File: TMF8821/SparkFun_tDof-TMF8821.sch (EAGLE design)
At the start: 27 parts, among them J4 QWIIC_RIGHT_ANGLE, J5 QWIIC_RIGHT_ANGLE

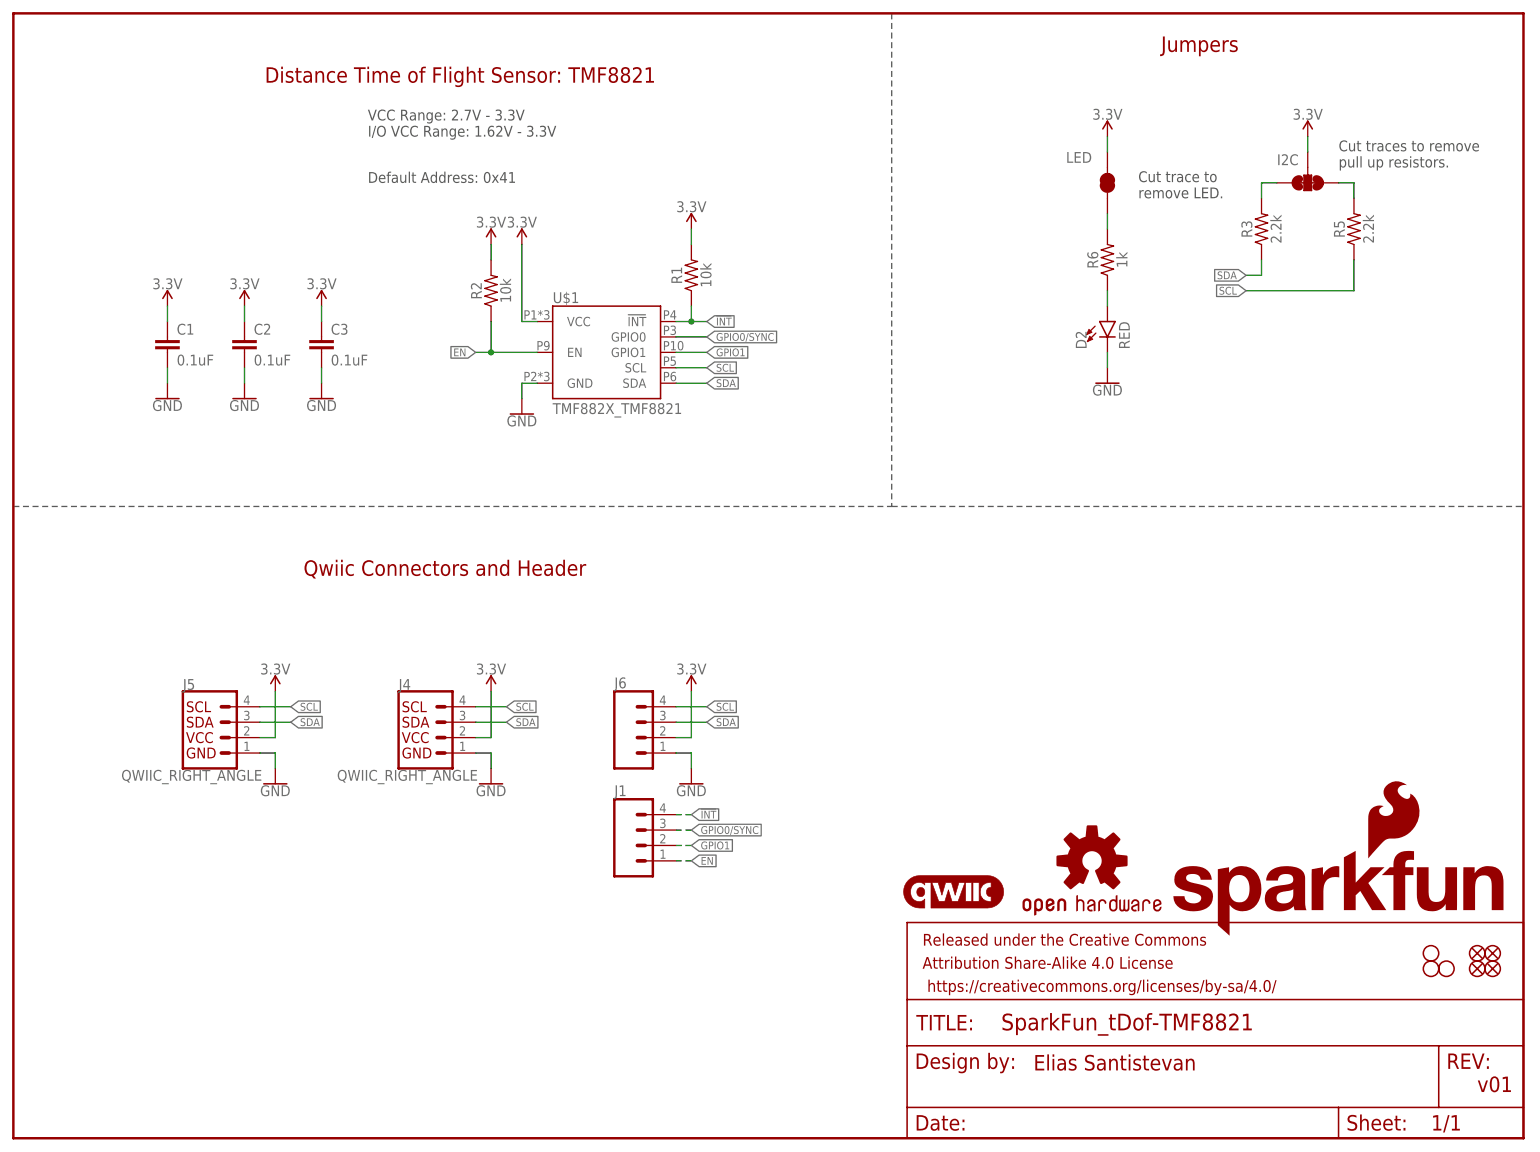
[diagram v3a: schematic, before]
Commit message: Removes old production files
* Removes old 8821 "HQ" variants
* Copies the 8820 and 8820 Mini variants
* Adjusts new 8820 copies to reference 8821 and replaces 8820 with 8821
* Updates Product Identifier jumpers to reflect changes
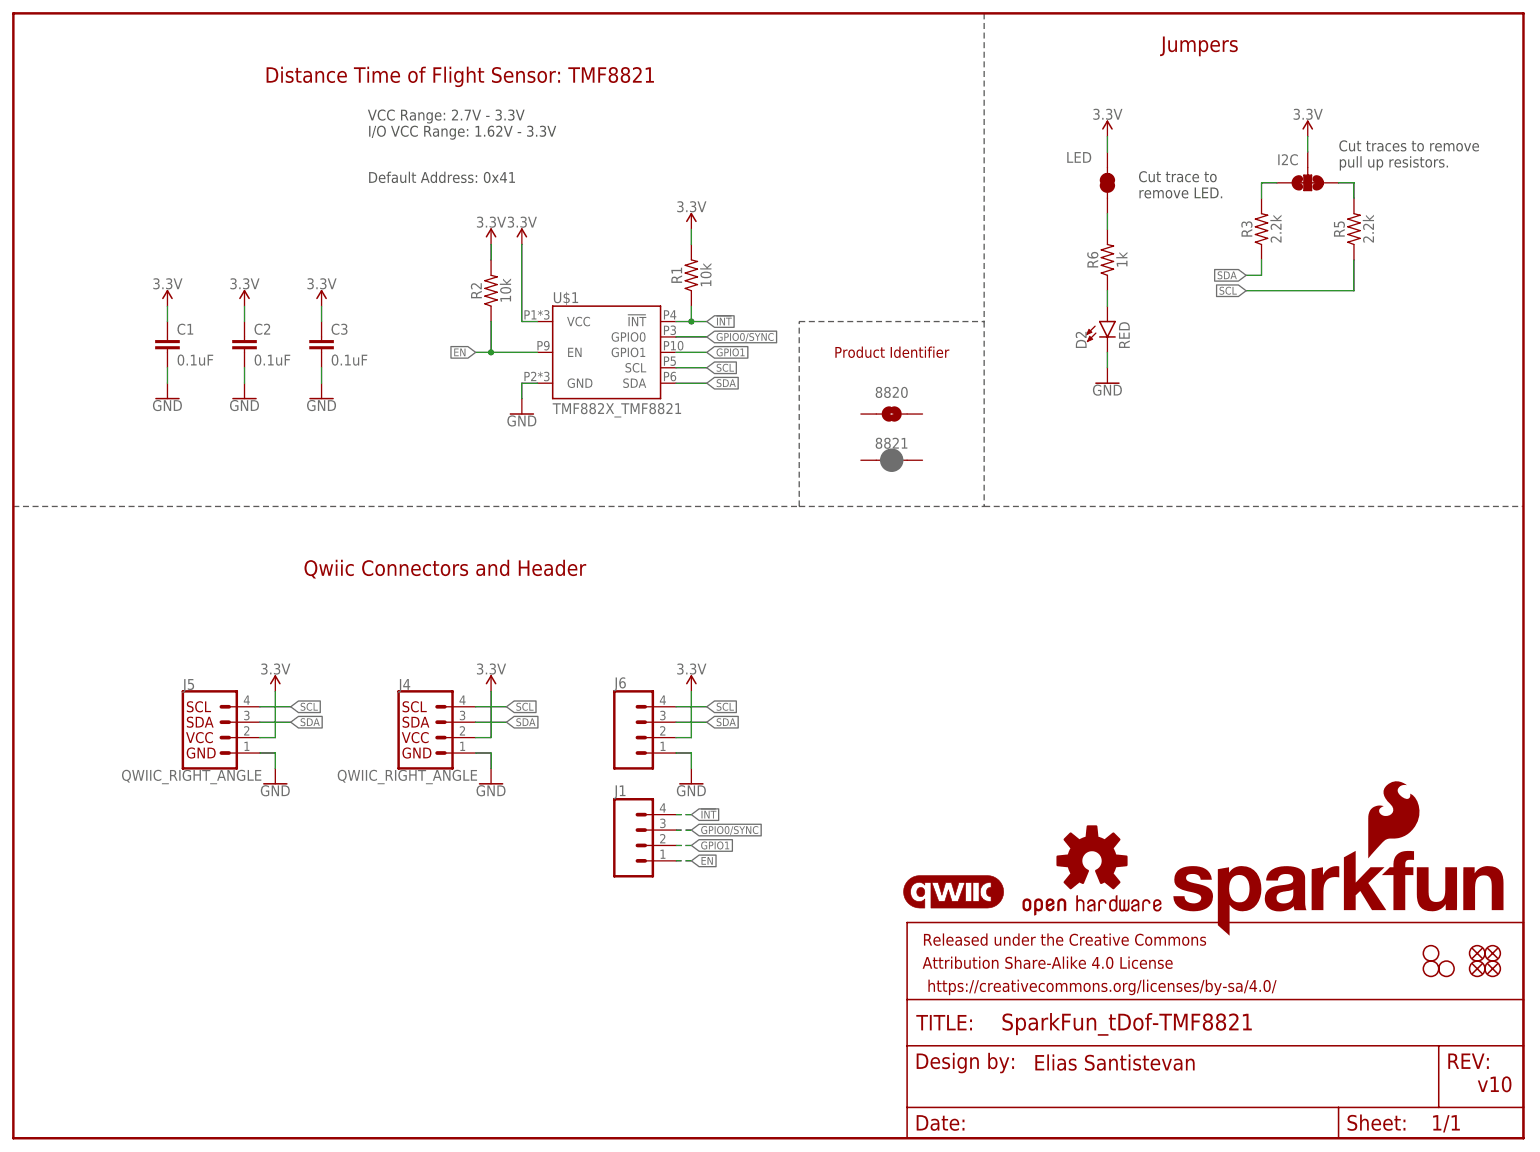
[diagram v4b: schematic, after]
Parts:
- added 8820: JUMPER-SMT_2_NO_SILK, SparkFun-Jumpers:JUMPER-SMT_2_NO_SILK
- added 8821: JUMPER-SMT_2_NC_PASTE_SILK, SparkFun-Jumpers:JUMPER-SMT_2_NC_PASTE_SILK
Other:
- note added: "Product Identifier"
- note added: "v10"
- note removed: "v01"
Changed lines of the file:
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@@
 <part name="SUPPLY11" library="SparkFun-PowerSymbols" deviceset="3.3V" device=""/>
 <part name="J1" library="SparkFun-Connectors" deviceset="CONN_04" device="1X04_NO_SILK_NO_POP"/>
+<part name="8820" library="SparkFun-Jumpers" deviceset="JUMPER-SMT_2_NO" device="_SILK" package3d_urn="urn:adsk.eagle:package:39279/1"/>
+<part name="8821" library="SparkFun-Jumpers" deviceset="JUMPER-SMT_2_NC_PASTE" device="_SILK" package3d_urn="urn:adsk.eagle:package:39282/1"/>
 </parts>
 <sheets>
 <sheet>
 <plain>
-<text x="241.3" y="7.62" size="2.54" layer="94" font="vector">v01</text>
+<text x="241.3" y="7.62" size="2.54" layer="94" font="vector">v10</text>
 <text x="71.12" y="93.98" size="2.54" layer="94" font="vector" align="center">Qwiic Connectors and Header</text>
 <text x="195.58" y="180.34" size="2.54" layer="94" font="vector" align="center">Jumpers</text>
@@
 <text x="168.148" y="11.176" size="2.54" layer="94" font="vector">Elias Santistevan</text>
 <text x="73.66" y="175.26" size="2.54" layer="94" font="vector" align="center">Distance Time of Flight Sensor: TMF8821</text>
-<wire x1="0" y1="104.14" x2="144.78" y2="104.14" width="0.2032" layer="97" style="longdash"/>
-<wire x1="144.78" y1="104.14" x2="248.92" y2="104.14" width="0.2032" layer="97" style="longdash"/>
-<wire x1="144.78" y1="185.42" x2="144.78" y2="104.14" width="0.2032" layer="97" style="longdash"/>
+<wire x1="0" y1="104.14" x2="129.54" y2="104.14" width="0.2032" layer="97" style="longdash"/>
+<wire x1="129.54" y1="104.14" x2="160.02" y2="104.14" width="0.2032" layer="97" style="longdash"/>
+<wire x1="160.02" y1="104.14" x2="248.92" y2="104.14" width="0.2032" layer="97" style="longdash"/>
+<wire x1="160.02" y1="185.42" x2="160.02" y2="134.62" width="0.2032" layer="97" style="longdash"/>
 <text x="58.42" y="165.1" size="1.778" layer="97" font="vector">VCC Range: 2.7V - 3.3V
 I/O VCC Range: 1.62V - 3.3V</text>
 <text x="58.42" y="157.48" size="1.778" layer="97" font="vector">Default Address: 0x41</text>
+<text x="144.78" y="129.54" size="1.778" layer="94" font="vector" align="center">Product Identifier</text>
+<wire x1="160.02" y1="134.62" x2="160.02" y2="104.14" width="0.2032" layer="97" style="longdash"/>
+<wire x1="129.54" y1="104.14" x2="129.54" y2="134.62" width="0.1524" layer="97" style="longdash"/>
+<wire x1="129.54" y1="134.62" x2="160.02" y2="134.62" width="0.1524" layer="97" style="longdash"/>
 </plain>
 <instances>
@@
 <attribute name="NAME" x="99.06" y="56.388" size="1.778" layer="95" font="vector"/>
 </instance>
+<instance part="8820" gate="G$1" x="144.78" y="119.38" smashed="yes">
+<attribute name="NAME" x="144.78" y="122.936" size="1.778" layer="95" font="vector" align="center"/>
+</instance>
+<instance part="8821" gate="G$1" x="144.78" y="111.76" smashed="yes">
+<attribute name="NAME" x="144.78" y="114.554" size="1.778" layer="95" font="vector" align="center"/>
+</instance>
 </instances>

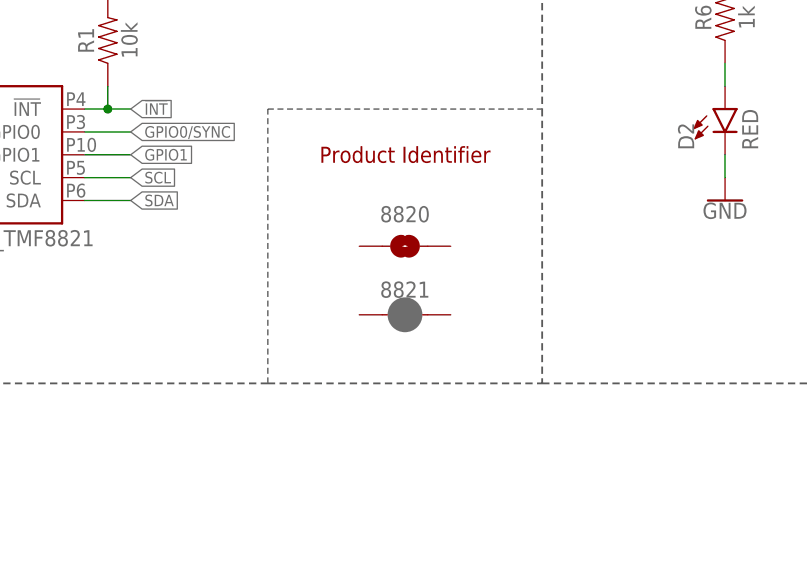
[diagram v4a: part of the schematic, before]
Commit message: Adds new product identifier pads to all designs, rolls 8820 version number to v10
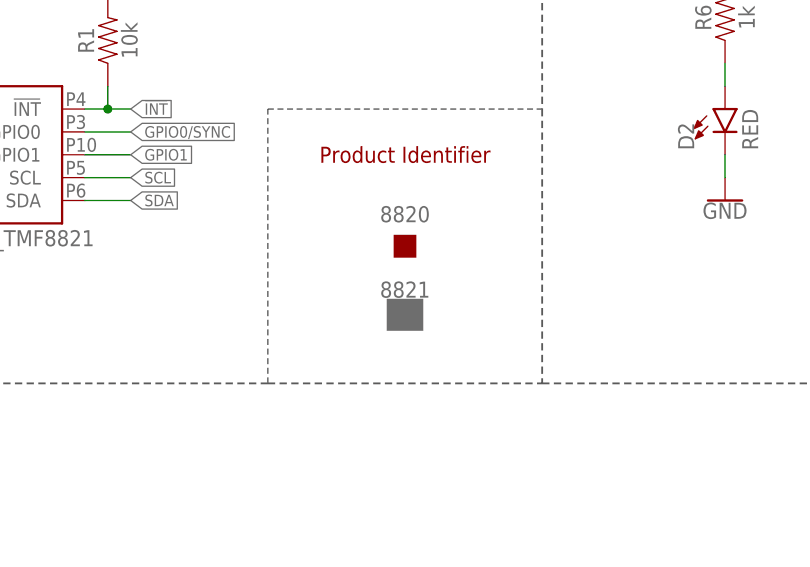
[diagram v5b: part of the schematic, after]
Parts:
- 8820: value JUMPER-SMT_2_NO_SILK -> PROD_ID_NO-PASTE_SILK; device SparkFun-Jumpers:JUMPER-SMT_2_NO_SILK -> SparkFun-Aesthetics:PROD_ID_NO-PASTE_SILK
- 8821: value JUMPER-SMT_2_NC_PASTE_SILK -> PROD_ID_PASTE_SILK; device SparkFun-Jumpers:JUMPER-SMT_2_NC_PASTE_SILK -> SparkFun-Aesthetics:PROD_ID_PASTE_SILK
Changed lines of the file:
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@@
 <part name="SUPPLY11" library="SparkFun-PowerSymbols" deviceset="3.3V" device=""/>
 <part name="J1" library="SparkFun-Connectors" deviceset="CONN_04" device="1X04_NO_SILK_NO_POP"/>
-<part name="8820" library="SparkFun-Jumpers" deviceset="JUMPER-SMT_2_NO" device="_SILK" package3d_urn="urn:adsk.eagle:package:39279/1"/>
-<part name="8821" library="SparkFun-Jumpers" deviceset="JUMPER-SMT_2_NC_PASTE" device="_SILK" package3d_urn="urn:adsk.eagle:package:39282/1"/>
+<part name="8820" library="SparkFun-Aesthetics" deviceset="PROD_ID_NO-PASTE" device="_SILK"/>
+<part name="8821" library="SparkFun-Aesthetics" deviceset="PROD_ID_PASTE" device="_SILK"/>
 </parts>
 <sheets>
